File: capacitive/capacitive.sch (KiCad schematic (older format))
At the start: 6 parts

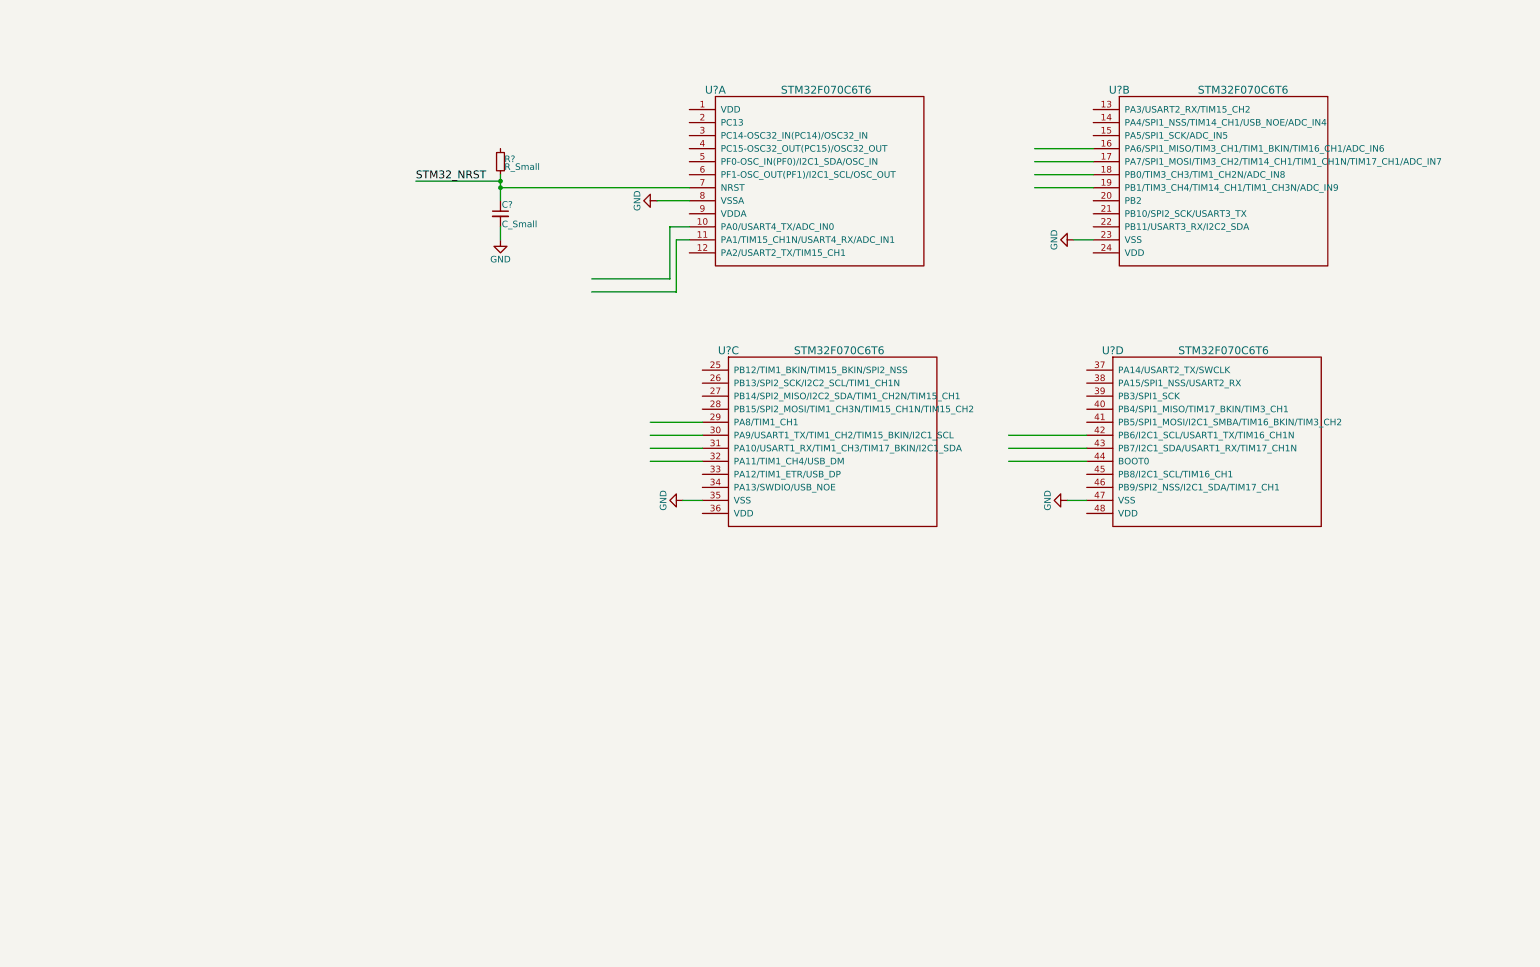
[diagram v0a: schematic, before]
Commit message: Schematic capture basically finished; TODO source and fp all components
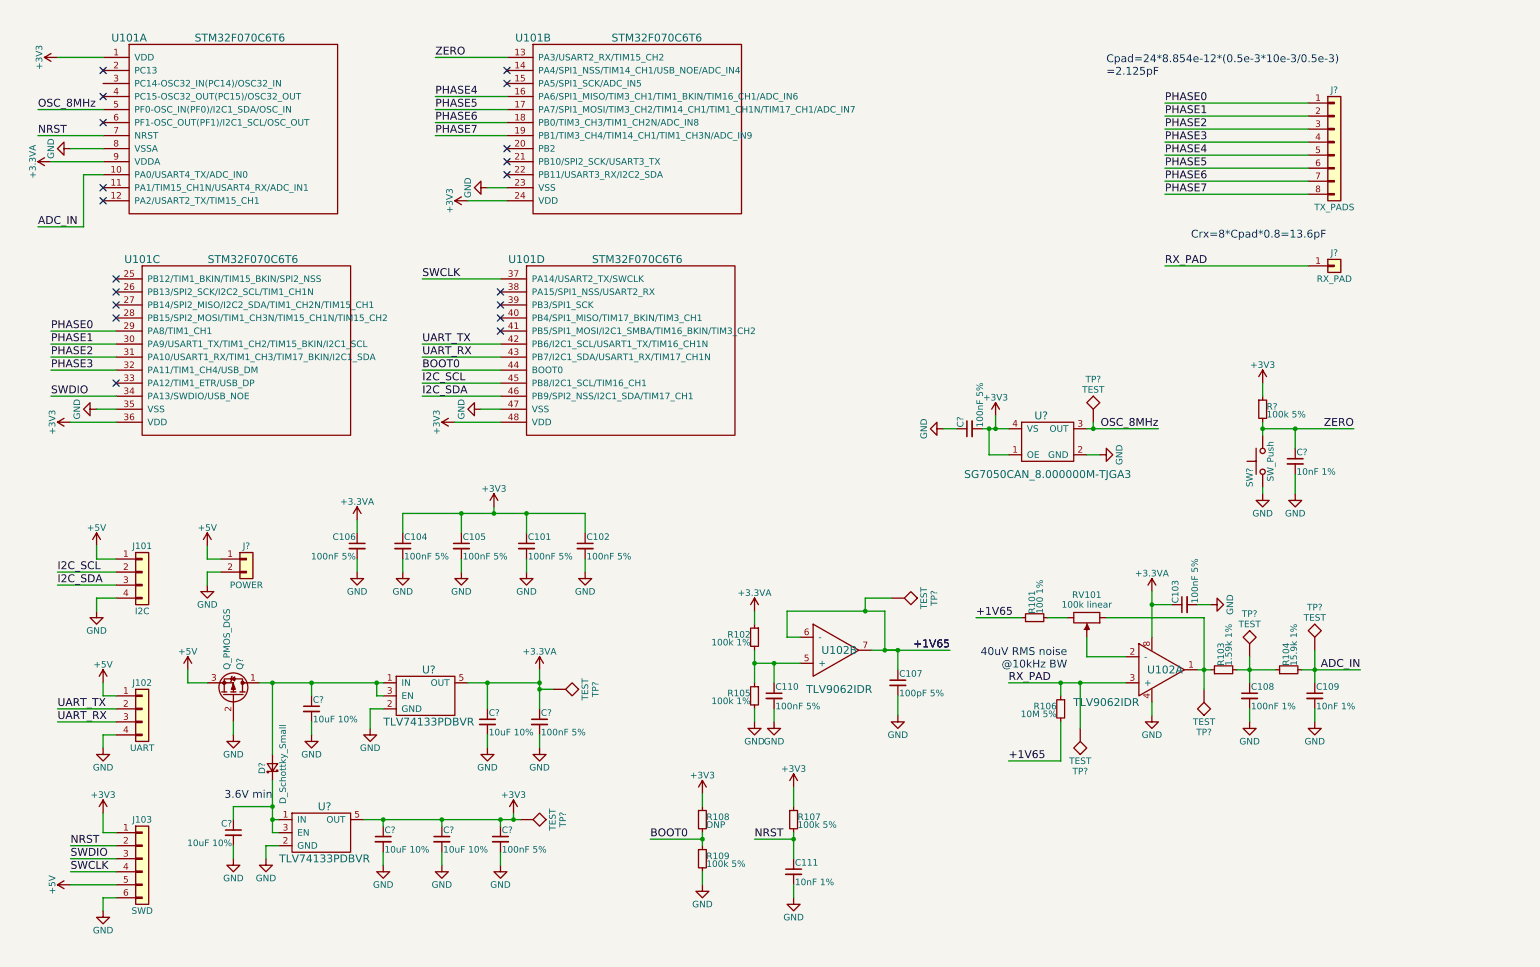
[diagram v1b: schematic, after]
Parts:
- removed C?: C_Small, symbol C_Small
- removed R?: R_Small, symbol R_Small
- removed U? (x4): STM32F070C6T6, symbol STM32F070C6T6
- added C101, C102, C103, C104, C105, C106, C110, C? (x3): 100nF 5%, symbol C_Small
- added C107: 100pF 5%, symbol C_Small
- added C108: 100nF 1%, symbol C_Small
- added C109, C111, C?: 10nF 1%, symbol C_Small
- added C? (x5): 10uF 10%, symbol C_Small
- added D?: D_Schottky_Small, symbol D_Schottky_Small
- added J101: I2C, symbol Conn_01x04
- added J102: UART, symbol Conn_01x04
- added J103: SWD, symbol Conn_01x06
- added J?: POWER, symbol Conn_01x02
- added J?: TX_PADS, symbol Conn_01x08
- added J?: RX_PAD, symbol Conn_01x01
- added Q?: Q_PMOS_DGS, symbol Q_PMOS_DGS
- added R101: 100 1%, symbol R_Small
- added R102, R105: 100k 1%, symbol R_Small
- added R103: 1.59k 1%, symbol R_Small
- added R104: 15.9k 1%, symbol R_Small
- added R106: 10M 5%, symbol R_Small
- added R107, R109, R?: 100k 5%, symbol R_Small
- added R108: DNP, symbol R_Small
- added RV101: 100k linear, symbol POT
- added SW?: SW_Push, symbol SW_Push
- added TP? (x8): TEST, symbol TEST
- added U101: STM32F070C6T6, symbol STM32F070C6T6
- added U102: TLV9062IDR, symbol TLV9062IDR
- added U? (x2): TLV74133PDBVR, symbol TLV74133PDBVR
- added U?: SG7050CAN_8.000000M-TJGA3, symbol SG7050CAN_8.000000M-TJGA3
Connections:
- net labels added: +1V65, +3.3VA, +3V3, +5V, ADC_IN, BOOT0, I2C_SCL, I2C_SDA, NRST, OSC_8MHz, PHASE0, PHASE1, PHASE2, PHASE3, PHASE4, PHASE5, PHASE6, PHASE7, RX_PAD, SWCLK, SWDIO, UART_RX, UART_TX, ZERO
- net labels removed: STM32_NRST
- wire segments 25 -> 168
- no-connect marks 0 -> 19
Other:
- note added: "3.6V min"
- note added: "40uV RMS noise\n@10kHz BW"
- note added: "Cpad=24*8.854e-12*(0.5e-3*10e-3/0.5e-3)\n=2.125pF"
- note added: "Crx=8*Cpad*0.8=13.6pF"

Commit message: Remove linear regulator and replace with resistor
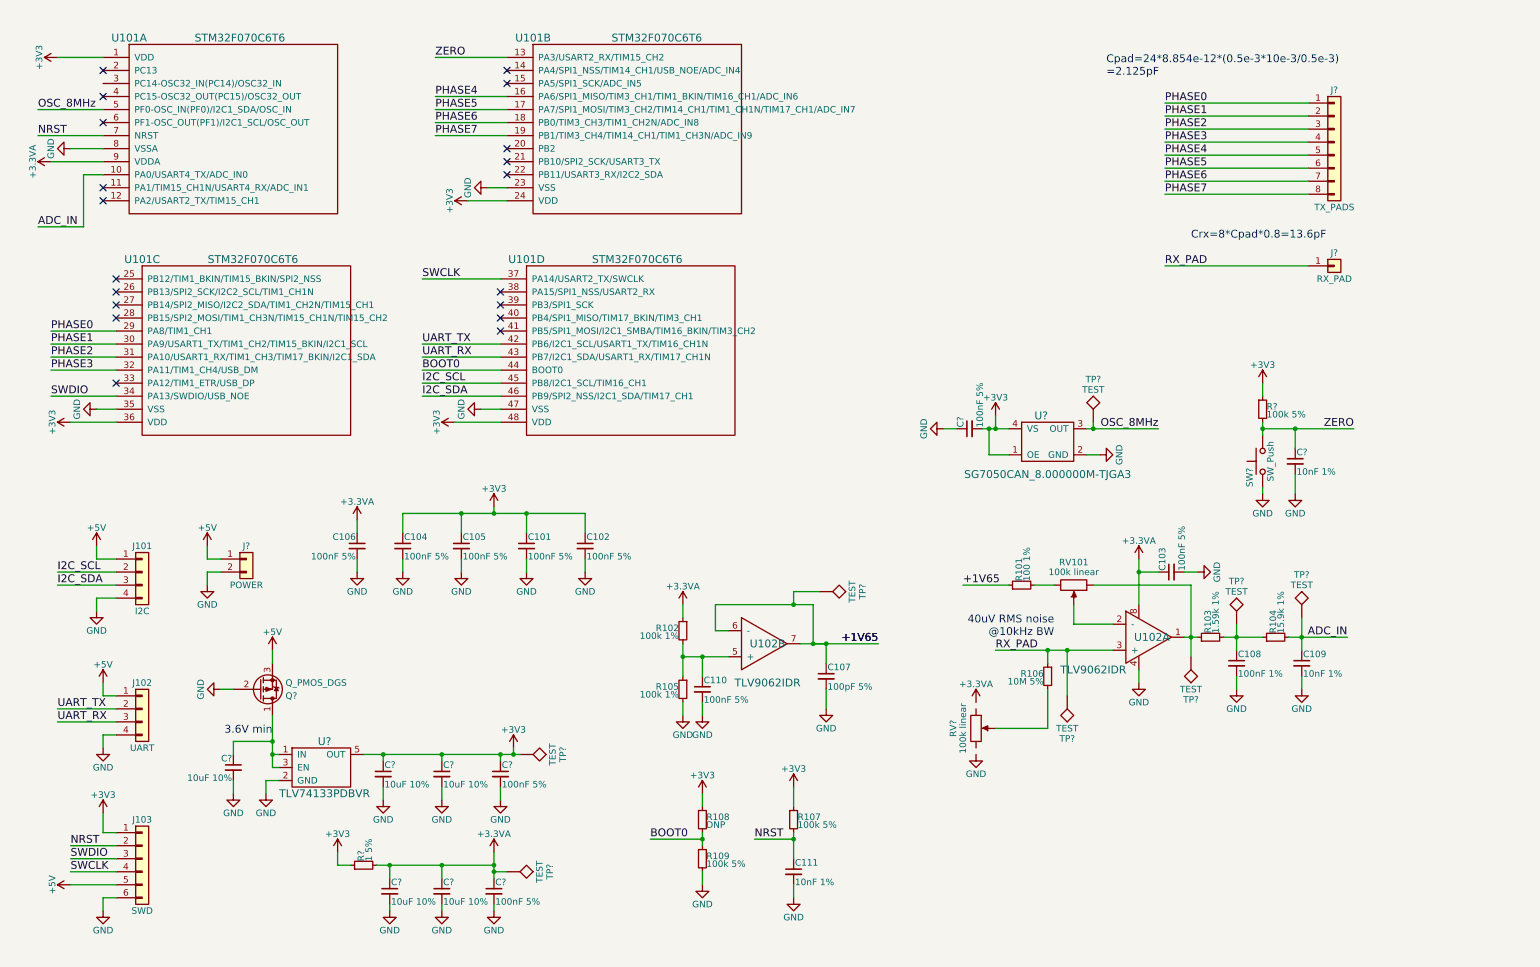
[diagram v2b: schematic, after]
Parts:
- removed D?: D_Schottky_Small, symbol D_Schottky_Small
- removed U?: TLV74133PDBVR, symbol TLV74133PDBVR
- added R?: 1 5%, symbol R_Small
- added RV?: 100k linear, symbol POT
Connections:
- net +1V65: no longer R106.2
- net +3.3VA: now also C?.1, R?.2
- net +3V3: now also R?.1
- net at C?.1, U?.1 (IN), U?.3 (EN): now also Q?.1 (D)
- new net: R106.2, RV?.2
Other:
- moved on the sheet: C103, C107, C108, C109, C110, C?, Q?, R101, R102, R103, R104, R105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
